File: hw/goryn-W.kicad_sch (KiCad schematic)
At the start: 4 parts, among them J1 Conn_01x34

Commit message: added DC-DC
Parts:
- added C1, C3: 10uF, AI6YP:C_0603_1608Metric, symbol AI6YP:C
- added C2, C4, C5, C6, C7: 22uF, AI6YP:C_0603_1608Metric, symbol AI6YP:C
- added L1, L2: 2.2uH, AI6YP:L_0805_2012Metric_Pad1.05x1.20mm_HandSolder, symbol AI6YP:L
- added R10: 68K, AI6YP:R_0603_1608Metric, symbol AI6YP:R
- added R11, R13: 15K, AI6YP:R_0603_1608Metric, symbol AI6YP:R
- added R12: 10K, AI6YP:R_0603_1608Metric, symbol AI6YP:R
- added U3, U4: MT3520B, AI6YP:SOT-23-5, symbol AI6YP:MT3520B
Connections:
- net +1V0: now also C4.1, C5.1, C7.1, L2.2, R12.1
- net +3V3: now also C2.1, C6.1, L1.2, R10.1
- net GND: now also C1.2, C2.2, C3.2, C4.2, C5.2, C6.2, C7.2, R11.2, R13.2, U3.2 (GND), U4.2 (GND)
- new net: L2.1, U4.3 (SW)
- new net: R12.2, R13.1, U4.5 (FB)
- new net: R10.2, R11.1, U3.5 (FB)
- new net: L1.1, U3.3 (SW)
- new net +5V: C1.1, C3.1, U3.1 (EN), U3.4 (VIN), U4.1 (EN), U4.4 (VIN)

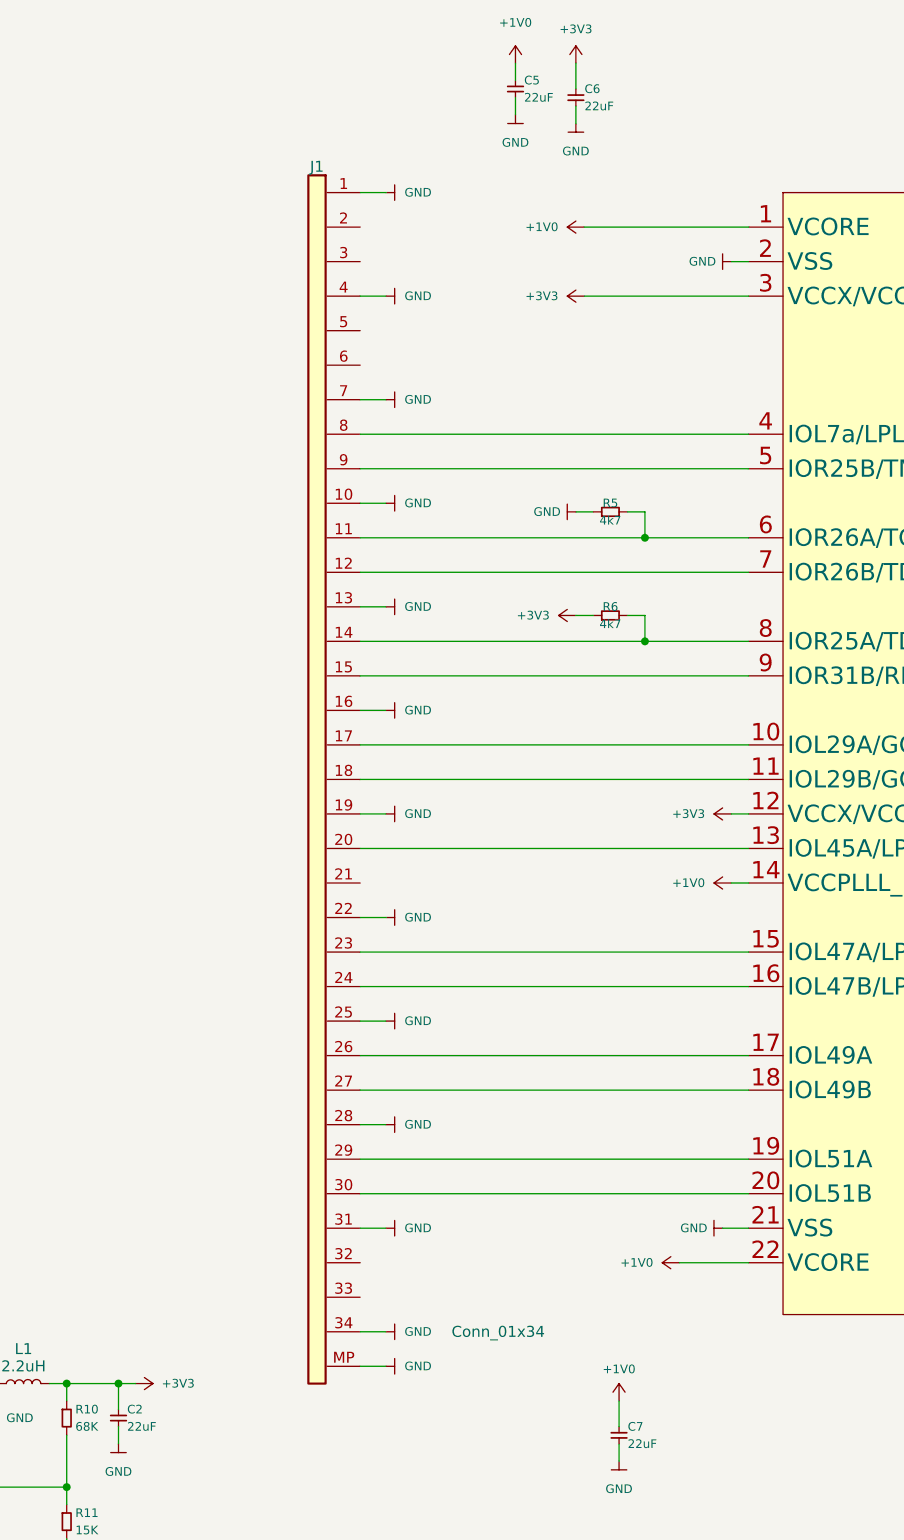
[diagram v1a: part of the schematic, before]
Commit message: FFC34 -> FFC30
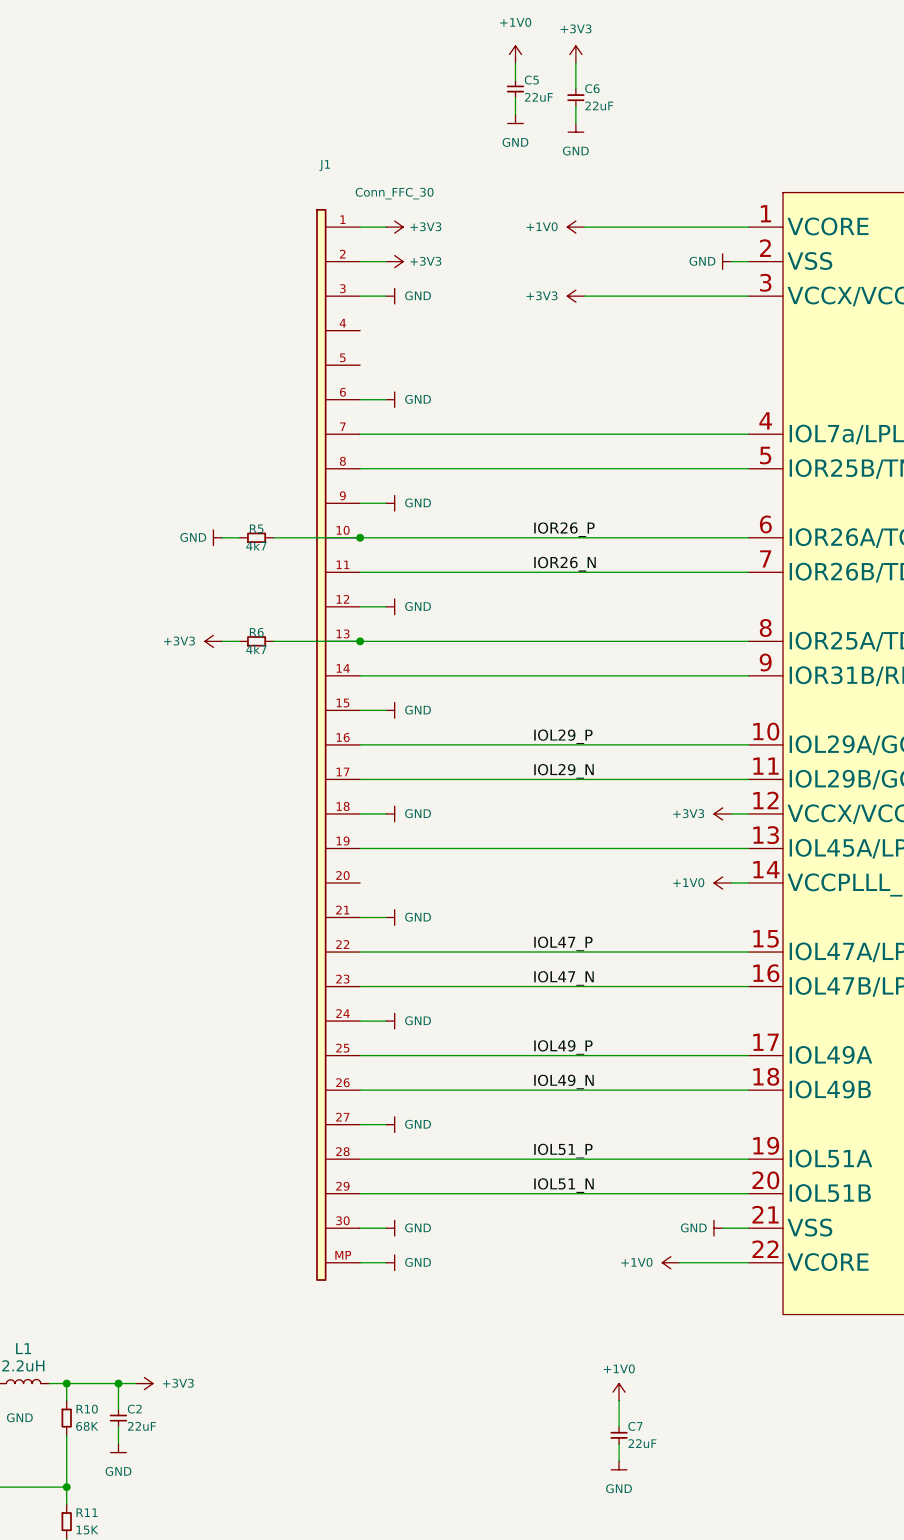
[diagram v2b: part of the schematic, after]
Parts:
- removed J1: Conn_01x34, AI6YP:Hirose_FH12-34S-0.5SH_1x34-1MP_P0.50mm_Horizontal, symbol AI6YP:Conn_01x34
- added J1: Conn_FFC_30, AI6YP:Hirose_FH12-30S-0.5SH_1x30-1MP_P0.50mm_Horizontal, symbol AI6YP:Conn_FFC_30
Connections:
- net +3V3: now also J1.1 (Pin_1), J1.2 (Pin_2)
- net GND: now also J1.12 (Pin_12), J1.15 (Pin_15), J1.18 (Pin_18), J1.21 (Pin_21), J1.24 (Pin_24), J1.27 (Pin_27), J1.3 (Pin_3), J1.30 (Pin_30), J1.6 (Pin_6), J1.9 (Pin_9), J1.MP (Pin_MP)
- net IOR26_P: now reaches R5.2, U1.6 (IOR26A/TCK)
- net IOR26_P: now also J1.10 (Pin_10)
- net at R6.2, U1.8 (IOR25A/TDO): now also J1.13 (Pin_13)
- net IOL29_P: now reaches U1.10 (IOL29A/GCLKT_6)
- net IOL29_P: now also J1.16 (Pin_16)
- net IOL29_N: now reaches U1.11 (IOL29B/GCLKC_6)
- net IOL29_N: now also J1.17 (Pin_17)
- net at U1.13 (IOL45A/LPLL2_T_in): now also J1.19 (Pin_19)
- net IOL47_P: now reaches U1.15 (IOL47A/LPLL2_T_fb)
- net IOL47_P: now also J1.22 (Pin_22)
- net IOL47_N: now reaches U1.16 (IOL47B/LPLL2_C_fb)
- net IOL47_N: now also J1.23 (Pin_23)
- net IOL49_P: now reaches U1.17 (IOL49A)
- net IOL49_P: now also J1.25 (Pin_25)
- net IOL49_N: now reaches U1.18 (IOL49B)
- net IOL49_N: now also J1.26 (Pin_26)
- net IOL51_P: now reaches U1.19 (IOL51A)
- net IOL51_P: now also J1.28 (Pin_28)
- net IOL51_N: now reaches U1.20 (IOL51B)
- net IOL51_N: now also J1.29 (Pin_29)
- net at U1.4 (IOL7a/LPLL1_T_in): now also J1.7 (Pin_7)
- net at U1.5 (IOR25B/TMS): now also J1.8 (Pin_8)
- net IOR26_N: now reaches U1.7 (IOR26B/TDI)
- net IOR26_N: now also J1.11 (Pin_11)
- net at U1.9 (IOR31B/RECONFIG_N): now also J1.14 (Pin_14)
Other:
- moved on the sheet: R5, R6

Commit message: happy kicad 8
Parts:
- added C14: 1uF, AI6YP:C_0603_1608Metric, symbol AI6YP:C
- added H1: MountingHole_M3, AI6YP:MountingHole_3.2mm_M3_Pad_Via, symbol AI6YP:MountingHole_M3
- added J5: Conn_Coaxial, AI6YP:U.FL_Hirose_U.FL-R-SMT-1_Vertical, symbol AI6YP:IPEX
- added J6: USB_C_Receptacle_USB2.0_16P, AI6YP:USB_C_Receptacle_GCT_USB4105-xx-A_16P_TopMnt_Horizontal, symbol AI6YP:USB_C_Receptacle_USB2.0_16P
- added R14, R15: 22, AI6YP:R_0603_1608Metric, symbol AI6YP:R
- added R16, R17: 0R, AI6YP:R_0603_1608Metric, symbol AI6YP:R
- added R18, R19: 5.1K, AI6YP:R_0603_1608Metric, symbol AI6YP:R
- added X1: osc_4pin_3.2_2.5, AI6YP:Crystal_SMD_EuroQuartz_MT-4Pin_3.2x2.5mm_HandSoldering, symbol AI6YP:osc_4pin_3.2_2.5
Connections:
- net +3V3: now also J1.30 (Pin_30), C14.1, X1.4 (V+); no longer J1.2 (Pin_2)
- net +5V: now also J6.A4 (VBUS), J6.A9 (VBUS), J6.B4 (VBUS), J6.B9 (VBUS)
- net GND: now also J1.11 (Pin_11), J1.14 (Pin_14), J1.17 (Pin_17), J1.2 (Pin_2), J1.20 (Pin_20), J1.23 (Pin_23), J1.26 (Pin_26), J1.29 (Pin_29), J1.5 (Pin_5), J1.8 (Pin_8), C14.2, H1.1, J5.2 (Ext), J6.A1 (GND), J6.A12 (GND), J6.B1 (GND), J6.B12 (GND), J6.S1 (SHIELD), R18.2, R19.2, X1.2 (GND); no longer J1.12 (Pin_12), J1.15 (Pin_15), J1.18 (Pin_18), J1.21 (Pin_21), J1.24 (Pin_24), J1.27 (Pin_27), J1.3 (Pin_3), J1.30 (Pin_30), J1.6 (Pin_6), J1.9 (Pin_9)
- net IOL29_N: now also J1.16 (Pin_16); no longer J1.17 (Pin_17)
- net IOL29_P: now also J1.15 (Pin_15); no longer J1.16 (Pin_16)
- net IOL47_N: now also J1.22 (Pin_22); no longer J1.23 (Pin_23)
- net IOL47_P: now also J1.21 (Pin_21); no longer J1.22 (Pin_22)
- net IOL49_N: now also J1.25 (Pin_25); no longer J1.26 (Pin_26)
- net IOL49_P: now also J1.24 (Pin_24); no longer J1.25 (Pin_25)
- net IOL51_N: now also J1.28 (Pin_28), R16.2; no longer J1.29 (Pin_29)
- net IOL51_P: now also J1.27 (Pin_27), R17.2; no longer J1.28 (Pin_28)
- net IOR26_N: now also J1.10 (Pin_10); no longer J1.11 (Pin_11)
- net IOR26_P: now also J1.9 (Pin_9); no longer J1.10 (Pin_10)
- net at R6.2, U1.8 (IOR25A/TDO): now also J1.12 (Pin_12); no longer J1.13 (Pin_13)
- net at U1.13 (IOL45A/LPLL2_T_in): now also J1.18 (Pin_18); no longer J1.19 (Pin_19)
- net at U1.4 (IOL7a/LPLL1_T_in): now also J1.6 (Pin_6), R14.2, R15.1; no longer J1.7 (Pin_7)
- net at U1.5 (IOR25B/TMS): now also J1.7 (Pin_7); no longer J1.8 (Pin_8)
- net at U1.9 (IOR31B/RECONFIG_N): now also J1.13 (Pin_13); no longer J1.14 (Pin_14)
- new net: J6.A7 (D-), J6.B7 (D-), R17.1
- new net: J5.1 (In), R15.2
- new net: J6.A5 (CC1), R18.1
- new net: R14.1, X1.3 (OUT)
- new net: J6.B5 (CC2), R19.1
- new net: J6.A6 (D+), J6.B6 (D+), R16.1
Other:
- moved on the sheet: C1, C2, C3, C4, C5, C6, C7, J1, L1, L2, R10, R11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

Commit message: finished routing
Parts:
- removed C1, C3: 10uF, AI6YP:C_0603_1608Metric, symbol AI6YP:C
- removed C2, C4, C7: 22uF, AI6YP:C_0603_1608Metric, symbol AI6YP:C
- removed H1: MountingHole_M3, AI6YP:MountingHole_3.2mm_M3_Pad_Via, symbol AI6YP:MountingHole_M3
- removed J6: USB_C_Receptacle_USB2.0_16P, AI6YP:USB_C_Receptacle_GCT_USB4105-xx-A_16P_TopMnt_Horizontal, symbol AI6YP:USB_C_Receptacle_USB2.0_16P
- removed L1, L2: 2.2uH, AI6YP:L_0805_2012Metric_Pad1.05x1.20mm_HandSolder, symbol AI6YP:L
- removed R10: 68K, AI6YP:R_0603_1608Metric, symbol AI6YP:R
- removed R11, R13: 15K, AI6YP:R_0603_1608Metric, symbol AI6YP:R
- removed R12: 10K, AI6YP:R_0603_1608Metric, symbol AI6YP:R
- removed R16, R17: 0R, AI6YP:R_0603_1608Metric, symbol AI6YP:R
- removed R18, R19: 5.1K, AI6YP:R_0603_1608Metric, symbol AI6YP:R
- removed U3, U4: MT3520B, AI6YP:SOT-23-5, symbol AI6YP:MT3520B
- added J30, J31, J32, J33: EMI-shield-clip-corner, AI6YP:EMI-shield-clip-corner, symbol AI6YP:EMI-shield-clip-corner
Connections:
- net GND: now also J30.1 (Pin_1), J31.1 (Pin_1), J32.1 (Pin_1), J33.1 (Pin_1)
- net at J1.6 (Pin_6), R14.2, U1.4 (IOL7A/LPLL1_T_in): now also R15.2; no longer R15.1
- net at J5.1 (In): now also R15.1; no longer R15.2
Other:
- moved on the sheet: C14, C5, C6, J1, J5, R14, R15, R5, R6, U1A, X1

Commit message: v1.0.0
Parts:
- removed J30, J31, J32, J33: EMI-shield-clip-corner, AI6YP:EMI-shield-clip-corner, symbol AI6YP:EMI-shield-clip-corner
- added H1, H2, H3, H4: MountingHole_M3, AI6YP:MountingHole_3.2mm_M3_Pad_Via, symbol AI6YP:MountingHole_M3
- U1: footprint AI6YP:QFN-88-10x10mm-P0.4mm-EP6.74x6.74mm -> AI6YP:GIWIN-QFN-88-10x10mm-P0.4mm-EP6.74x6.74mm
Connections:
- net GND: now also H1.1, H2.1, H3.1, H4.1
